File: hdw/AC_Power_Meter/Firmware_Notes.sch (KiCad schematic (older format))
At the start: 0 parts

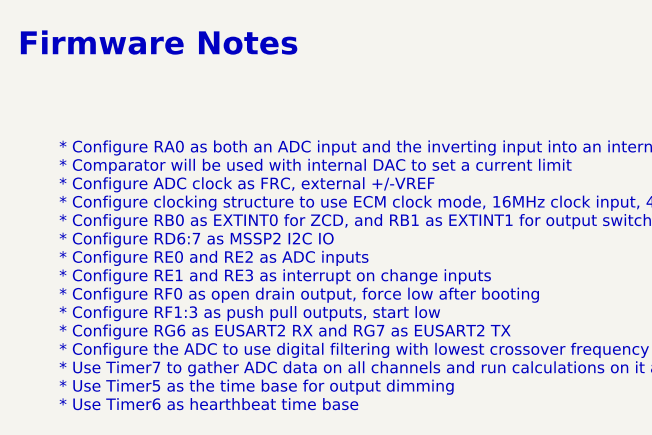
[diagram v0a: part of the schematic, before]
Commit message: Finished placing parts
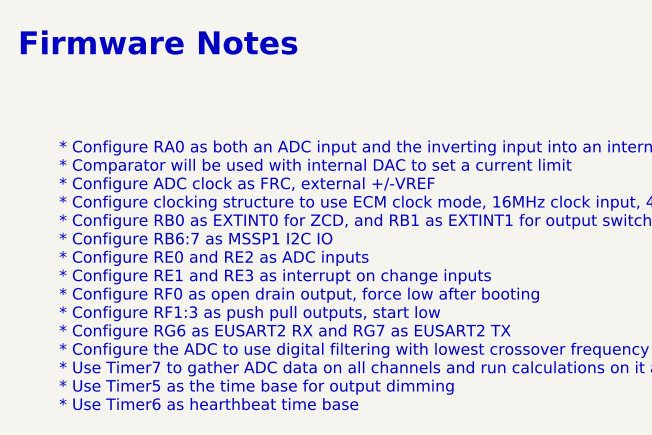
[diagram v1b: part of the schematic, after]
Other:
- note added: "* Configure RA0 as both an ADC input and the inverting input into an internal comparator\n* Comparator will be used with internal DAC to set a current limit\n* Configure ADC clock as FRC, external +/-VREF\n* Configure clocking structure to use ECM clock mode, 16MHz clock input, 4xPLL = 64MHz SYSCLK\n* Configure RB0 as EXTINT0 for ZCD, and RB1 as EXTINT1 for output switching\n* Configure RB6:7 as 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"
- note removed: "* Configure RA0 as both an ADC input and the inverting input into an internal comparator\n* Comparator will be used with internal DAC to set a current limit\n* Configure ADC clock as FRC, external +/-VREF\n* Configure clocking structure to use ECM clock mode, 16MHz clock input, 4xPLL = 64MHz SYSCLK\n* Configure RB0 as EXTINT0 for ZCD, and RB1 as EXTINT1 for output switching\n* Configure RD6:7 as 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"
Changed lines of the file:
@@
 $EndComp
 Text Notes 720  2240 0    50   ~ 0
-* Configure RA0 as both an ADC input and the inverting input into an internal comparator\n* Comparator will be used with internal DAC to set a current limit\n* Configure ADC clock as FRC, external +/-VREF\n* Configure clocking structure to use ECM clock mode, 16MHz clock input, 4xPLL = 64MHz SYSCLK\n* Configure RB0 as EXTINT0 for ZCD, and RB1 as EXTINT1 for output switching\n* Configure RD6:7 as MSSP2 I2C IO\n* Configure RE0 and RE2 as ADC inputs\n* Configure RE1 and RE3 as interrupt on change inputs\n* Configure RF0 as open drain output, force low after booting\n* Configure RF1:3 as push pull outputs, start low\n* Configure RG6 as EUSART2 RX and RG7 as EUSART2 TX\n* Configure the ADC to use digital filtering with lowest crossover frequency\n* Use Timer7 to gather ADC data on all channels and run calculations on it at a fixed time base\n* Use Timer5 as the time base for output dimming\n* Use Timer6 as hearthbeat time base
+* Configure RA0 as both an ADC input and the inverting input into an internal comparator\n* Comparator will be used with internal DAC to set a current limit\n* Configure ADC clock as FRC, external +/-VREF\n* Configure clocking structure to use ECM clock mode, 16MHz clock input, 4xPLL = 64MHz SYSCLK\n* Configure RB0 as EXTINT0 for ZCD, and RB1 as EXTINT1 for output switching\n* Configure RB6:7 as MSSP1 I2C IO\n* Configure RE0 and RE2 as ADC inputs\n* Configure RE1 and RE3 as interrupt on change inputs\n* Configure RF0 as open drain output, force low after booting\n* Configure RF1:3 as push pull outputs, start low\n* Configure RG6 as EUSART2 RX and RG7 as EUSART2 TX\n* Configure the ADC to use digital filtering with lowest crossover frequency\n* Use Timer7 to gather ADC data on all channels and run calculations on it at a fixed time base\n* Use Timer5 as the time base for output dimming\n* Use Timer6 as hearthbeat time base
 $EndSCHEMATC

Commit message: Finished routing, adding bells and whistles
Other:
- note added: "* Configure RA0 as both an ADC input and the inverting input into an internal comparator\n* Comparator will be used with internal DAC to set a current limit\n* Configure ADC clock as FRC, external +/-VREF\n* Configure clocking structure to use ECM clock mode, 16MHz clock input, 4xPLL = 64MHz SYSCLK\n* Configure RA4 as an ADC input\n* Configure RA5 as EXTINT0 for ZCD\n* Configure RB0 as EXTINT1 fo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"
- note removed: "* Configure RA0 as both an ADC input and the inverting input into an internal comparator\n* Comparator will be used with internal DAC to set a current limit\n* Configure ADC clock as FRC, external +/-VREF\n* Configure clocking structure to use ECM clock mode, 16MHz clock input, 4xPLL = 64MHz SYSCLK\n* Configure RB0 as EXTINT0 for ZCD, and RB1 as EXTINT1 for output switching\n* Configure RB6:7 as 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"
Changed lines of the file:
@@
 $EndComp
 Text Notes 720  2240 0    50   ~ 0
-* Configure RA0 as both an ADC input and the inverting input into an internal comparator\n* Comparator will be used with internal DAC to set a current limit\n* Configure ADC clock as FRC, external +/-VREF\n* Configure clocking structure to use ECM clock mode, 16MHz clock input, 4xPLL = 64MHz SYSCLK\n* Configure RB0 as EXTINT0 for ZCD, and RB1 as EXTINT1 for output switching\n* Configure RB6:7 as MSSP1 I2C IO\n* Configure RE0 and RE2 as ADC inputs\n* Configure RE1 and RE3 as interrupt on change inputs\n* Configure RF0 as open drain output, force low after booting\n* Configure RF1:3 as push pull outputs, start low\n* Configure RG6 as EUSART2 RX and RG7 as EUSART2 TX\n* Configure the ADC to use digital filtering with lowest crossover frequency\n* Use Timer7 to gather ADC data on all channels and run calculations on it at a fixed time base\n* Use Timer5 as the time base for output dimming\n* Use Timer6 as hearthbeat time base
+* Configure RA0 as both an ADC input and the inverting input into an internal comparator\n* Comparator will be used with internal DAC to set a current limit\n* Configure ADC clock as FRC, external +/-VREF\n* Configure clocking structure to use ECM clock mode, 16MHz clock input, 4xPLL = 64MHz SYSCLK\n* Configure RA4 as an ADC input\n* Configure RA5 as EXTINT0 for ZCD\n* Configure RB0 as EXTINT1 for output switching\n* Configure RB6:7 as MSSP1 I2C IO\n* Configure RC2 and RC3 as interrupt on change inputs\n* Configure RE2 as an ADC input\n* Configure RF0 as open drain output, force low after booting\n* Configure RF1:3 as push pull outputs, start low\n* Configure RG6 as EUSART2 RX and RG7 as EUSART2 TX\n* Configure the ADC to use digital filtering with lowest crossover frequency\n* Use Timer7 to gather ADC data on all channels and run calculations on it at a fixed time base\n* Use Timer5 as the time base for output dimming\n* Use Timer6 as hearthbeat time base
 $EndSCHEMATC
